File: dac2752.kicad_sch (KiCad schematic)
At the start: 57 parts, among them U61 OPA2388D, U62 OPA2388D, U63 OPA2197xD, U64 OPA2197xD

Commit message: More work in progres
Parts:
- removed C?: 10n, symbol Device:C
- added C?: 100p, symbol Device:C
- C?: value 33n -> 10n
- R? (x2): value 1k -> 3k3
- gave numbers to parts that had none: 15
- renumbered U61 to U32, U63 to U33, U62 to U35, U64 to U36
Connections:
- net -5VS is gone; now on net REFB: U31.35 (REFB)
- net -18V: no longer U301.4 (V-)
- net at R?.1: now also C?.1; no longer C?.2
- net at U31.31 (RINB): now also U34.6 (-)
- net at R?.1, R?.1, U31.32 (RINB): now also U34.7
- net at R?.1, R?.2, U35.1: now also C?.2
- net at R?.1, R?.2, U35.2 (-): now also C?.1
- net Ref5V: now reaches U34.5 (+)
- net Ref5V: now also U34.3 (+)
- net -5VF renamed REFB
- net REFB: now also C?.2; no longer C?.1
- net AGND renamed GND
- net GND: now also U33.3 (+); no longer U36.3 (+)
- net PGND renamed GNDPWR
- net GNDPWR: now also U301.4 (V-), U36.3 (+); no longer U33.3 (+)
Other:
- moved on the sheet: C301, C?, R?, U301C, U32A, U33A, U34B, U35A, U36A

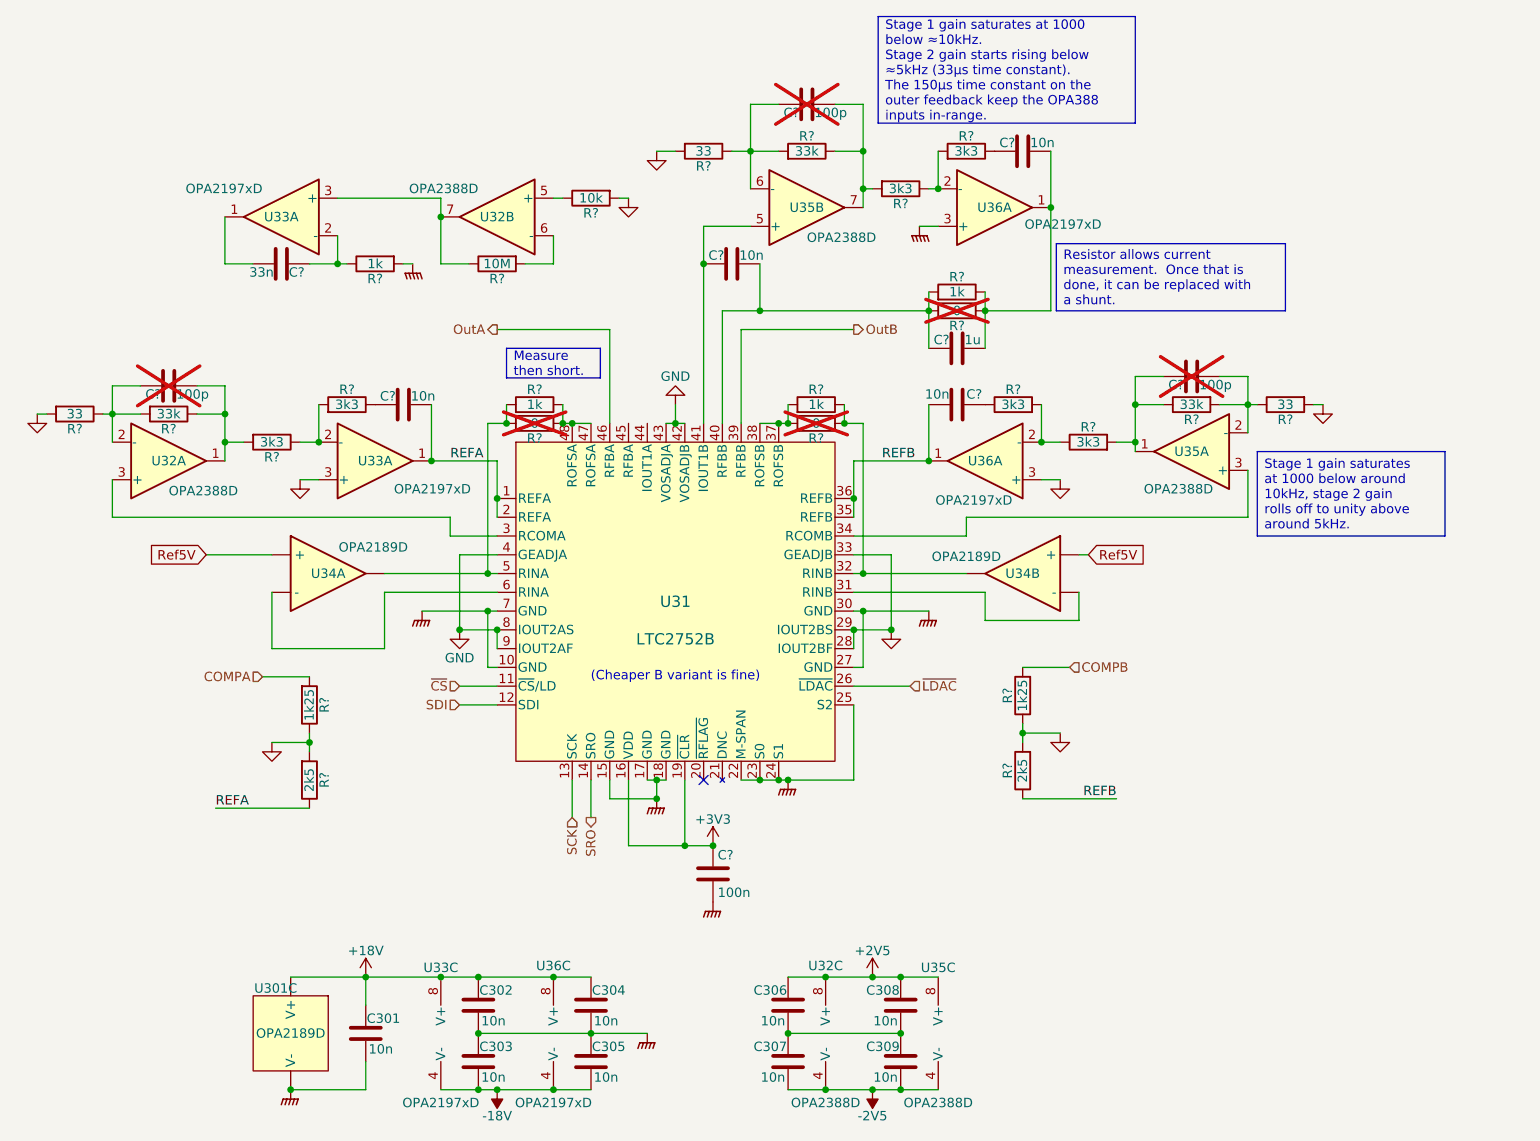
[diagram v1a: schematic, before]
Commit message: Analog side is more or less complete.
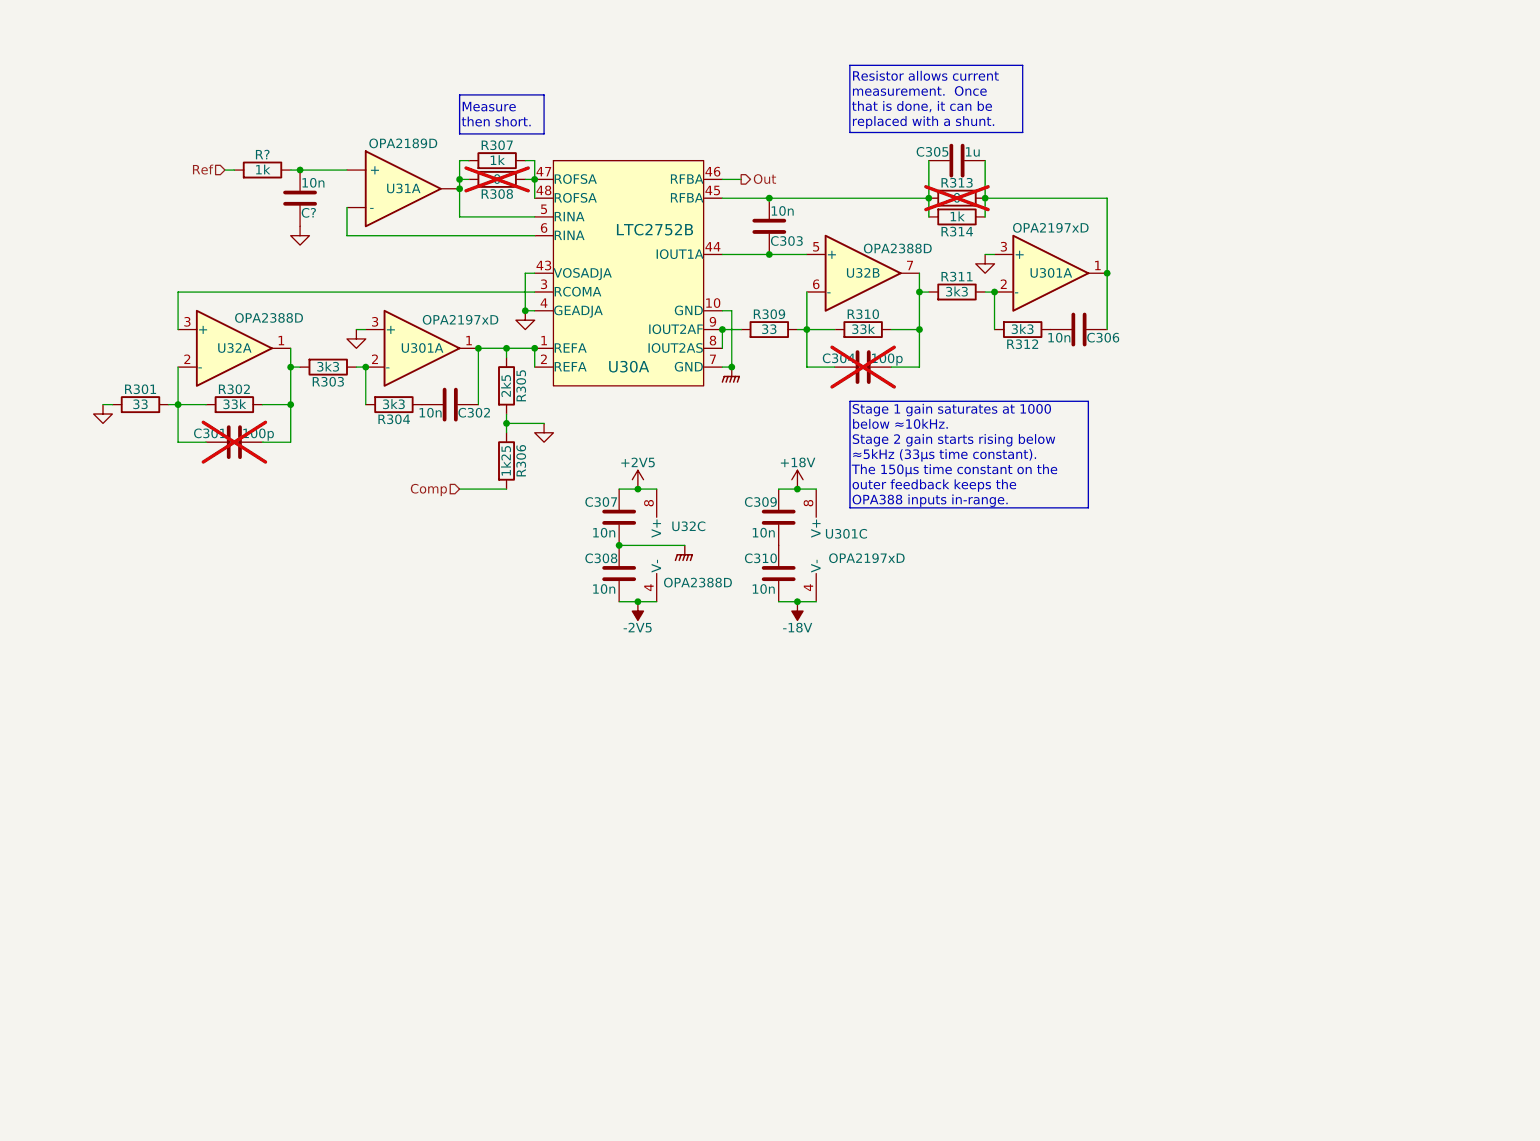
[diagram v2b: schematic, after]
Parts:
- removed C301, C304, C308, C309, C? (x3): 10n, symbol Device:C
- removed C?: 100n, symbol Device:C
- removed C?: 33n, symbol Device:C
- removed C?: 100p, symbol Device:C
- removed C?: 1u, symbol Device:C
- removed R? (x3): 1k, symbol Device:R
- removed R? (x3): 3k3, symbol Device:R
- removed R? (x2): 33k, symbol Device:R
- removed R?: 1k25, symbol Device:R
- removed R?: 10M, symbol Device:R
- removed R?: 33, symbol Device:R
- removed R?: 2k5, symbol Device:R
- removed R?: 10k, symbol Device:R
- removed R? (x2): 0, symbol Device:R
- removed U301: OPA2189D, Package_SO:SOIC-8_3.9x4.9mm_P1.27mm, symbol Parts:OPA2189D
- removed U31: LTC2752B, LQFP-48_LX_LIT, symbol Parts:LTC2752B
- removed unit 2 of U32
- removed unit 1 of U33 (x2)
- removed unit 2 of U34
- removed unit 3 of U35
- removed unit 1 of U35
- removed U36 (x2): OPA2197xD, Package_SO:SOIC-8_3.9x4.9mm_P1.27mm, symbol Amplifier_Operational:OPA2197xD
- added C302, C306, C?: 10n, symbol Device:C
- added R310: 33k, symbol Device:R
- added R312: 3k3, symbol Device:R
- added R313: 0, symbol Device:R
- added R314, R?: 1k, symbol Device:R
- added U30: LTC2752B, Package_QFP:LQFP-48_7x7mm_P0.5mm, symbol Parts:LTC2752B_split
- added unit 1 of U301 (x2)
- C305: value 10n -> 1u
- gave numbers to parts that had none: 13
- renumbered C306 to C307, C307 to C308, C302 to C309, C303 to C310, U33 to U301, U34 to U31, U35 to U32
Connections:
- net -18V: no longer C305.2
- net GND: now also C?.2, U30.4 (GEADJA), U30.43 (VOSADJA), U301.3 (+), U301.3 (+); no longer R309.2
- net GNDPWR: now also C307.2, C308.1, U30.10 (GND), U30.7 (GND); no longer C305.1, C309.2, C310.1
- net at U32.3 (+): now also U30.3 (RCOMA)
- net at R303.1, R304.2: now also U301.2 (-)
- net at C303.1: now also C305.2, R313.2, R314.2, U30.45 (RFBA)
- net at C303.2, U32.5 (+): now also U30.44 (IOUT1A)
- net at C304.2, R309.1, U32.6 (-): now also R310.2
- net at C304.1, R311.2, U32.7: now also R310.1
- net at R307.1, R308.1: now also U30.47 (ROFSA), U30.48 (ROFSA)
- net at R307.2, R308.2, U31.1: now also U30.5 (RINA)
- net at U31.2 (-): now also U30.6 (RINA)
- net at R304.1: now also C302.2
- net at R311.1: now also R312.2, U301.2 (-)
- net COMPA renamed Comp
- net REFA: no longer names the net of R305.1
- net REFA: now also C302.1, U30.1 (REFA), U30.2 (REFA), U301.1
- net Ref5V: no longer names the net of U31.3 (+)
- net Ref5V: now also C?.1, R?.1
- new net: C305.1, C306.1, R313.1, R314.1, U301.1
- new net: R309.2, U30.8 (IOUT2AS), U30.9 (IOUT2AF)
- new net: C309.2, C310.1
- new net: C306.2, R312.1
- new net Out: U30.46 (RFBA)
- new net Ref: R?.2
- no-connect marks 1 -> 0
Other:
- note removed: "(Cheaper B variant is fine)"
- moved on the sheet: C301, C303, C304, C307, C308, C309, C310, R301, R302, R303, R304, R305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

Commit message: Little simplifications etc.
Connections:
- net GND: now also R309.2, U30.8 (IOUT2AS), U30.9 (IOUT2AF)
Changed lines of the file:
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@@
 	(generator_version "9.0")
 	(paper "A4")
+	(text_box "Connect to IOUT2"
+		(exclude_from_sim no)
+		(at 104.9655 81.8459 0)
+		(size 10.6044 4.514)
+		(margins 0.9525 0.9525 0.9525 0.9525)
+		(stroke
+			(width 0)
+			(type default)
+		)
+		(fill
+			(type none)
+		)
+		(effects
+			(font
+				(size 1.27 1.27)
+			)
+			(justify left)
+		)
+	)
 	(text_box "Measure then short."
 		(exclude_from_sim no)
@@
 	)
 	(junction
+		(at 127 73.66)
+		(diameter 0)
+		(color 0 0 0 0)
+	)
+	(junction
 		(at 97.79 83.82)
 		(diameter 0)
@@
 	)
 	(junction
-		(at 128.27 76.2)
-		(diameter 0)
-		(color 0 0 0 0)
-	)
-	(junction
 		(at 163.83 66.04)
 		(diameter 0)
@@
 	(wire
 		(pts
+			(xy 127 73.66) (xy 130.81 73.66)
+		)
+		(stroke
+			(width 0)
+			(type default)
+		)
+	)
+	(wire
+		(pts
 			(xy 149.86 76.2) (xy 153.67 76.2)
 		)
@@
 	(wire
 		(pts
-			(xy 128.27 68.58) (xy 128.27 76.2)
-		)
-		(stroke
-			(width 0)
-			(type default)
-		)
-	)
-	(wire
-		(pts
 			(xy 101.6 68.58) (xy 100.33 68.58)
 		)
@@
 	)
 	(symbol
+		(lib_id "power:GNDPWR")
+		(at 128.27 68.58 0)
+		(unit 1)
+		(exclude_from_sim no)
+		(in_bom yes)
+		(on_board yes)
+		(dnp no)
+		(property "Reference" "#PWR0561"
+			(at 128.27 74.93 0)
+			(effects
+				(font
+					(size 1.27 1.27)
+				)
+				(hide yes)
+			)
+		)
+		(property "Value" "GNDPWR"
+			(at 128.27 71.882 0)
+			(effects
+				(font
+					(size 1.27 1.27)
+				)
+				(hide yes)
+			)
+		)
+		(property "Footprint" ""
+			(at 128.27 69.85 0)
+			(effects
+				(font
+					(size 1.27 1.27)
+				)
+				(hide yes)
+			)
+		)
+		(property "Datasheet" ""
+			(at 128.27 69.85 0)
+			(effects
+				(font
+					(size 1.27 1.27)
+				)
+				(hide yes)
+			)
+		)
+		(property "Description" "Power symbol creates a global label with name \"GNDPWR\" , global ground"
+			(at 128.27 68.58 0)
+			(effects
+				(font
+					(size 1.27 1.27)
+				)
+				(hide yes)
+			)
+		)
+		(pin "1"
+		)
+		(instances
+			(project "lincal"
+				(path "/b054cef4-39e3-49d8-aff0-7ba5a206c187/361a423f-d05f-4f8b-bc28-600b62434109"
+					(reference "#PWR0562")
+					(unit 1)
+				)
+				(path "/b054cef4-39e3-49d8-aff0-7ba5a206c187/460d889b-fb9b-4b3e-8128-6fba79ce7ab4"
+					(reference "#PWR0563")
+					(unit 1)
+				)
+				(path "/b054cef4-39e3-49d8-aff0-7ba5a206c187/aeb3a378-4287-41b1-9e33-8dbd035c4d66"
+					(reference "#PWR0564")
+					(unit 1)
+				)
+				(path "/b054cef4-39e3-49d8-aff0-7ba5a206c187/f2e682f2-52ca-4ed0-8a7d-aeb09fbc9914"
+					(reference "#PWR0561")
+					(unit 1)
+				)
+			)
+		)
+	)
+	(symbol
 		(lib_id "Device:R")
 		(at 97.79 78.74 0)
@@
 					(unit 1)
 				)
+			)
+		)
+	)
+	(symbol
+		(lib_id "power:GND")
+		(at 130.81 73.66 0)
+		(mirror y)
+		(unit 1)
+		(exclude_from_sim no)
+		(in_bom yes)
+		(on_board yes)
+		(dnp no)
+		(property "Reference" "#PWR0565"
+			(at 130.81 80.01 0)
+			(effects
+				(font
+					(size 1.27 1.27)
+				)
+				(hide yes)
+			)
+		)
+		(property "Value" "GND"
+			(at 130.81 77.47 0)
+			(effects
+				(font
+					(size 1.27 1.27)
+				)
+				(hide yes)
+			)
+		)
+		(property "Footprint" ""
+			(at 130.81 73.66 0)
+			(effects
+				(font
+					(size 1.27 1.27)
+				)
+				(hide yes)
+			)
+		)
+		(property "Datasheet" ""
+			(at 130.81 73.66 0)
+			(effects
+				(font
+					(size 1.27 1.27)
+				)
+				(hide yes)
+			)
+		)
+		(property "Description" "Power symbol creates a global label with name \"GND\" , ground"
+			(at 130.81 73.66 0)
+			(effects
+				(font
+					(size 1.27 1.27)
+				)
+				(hide yes)
+			)
+		)
+		(pin "1"
+		)
+		(instances
+			(project "lincal"
+				(path "/b054cef4-39e3-49d8-aff0-7ba5a206c187/361a423f-d05f-4f8b-bc28-600b62434109"
+					(reference "#PWR0566")
+					(unit 1)
+				)
+				(path "/b054cef4-39e3-49d8-aff0-7ba5a206c187/460d889b-fb9b-4b3e-8128-6fba79ce7ab4"
+					(reference "#PWR0567")
+					(unit 1)
+				)
+				(path "/b054cef4-39e3-49d8-aff0-7ba5a206c187/aeb3a378-4287-41b1-9e33-8dbd035c4d66"
+					(reference "#PWR0568")
+					(unit 1)
+				)
+				(path "/b054cef4-39e3-49d8-aff0-7ba5a206c187/f2e682f2-52ca-4ed0-8a7d-aeb09fbc9914"
+					(reference "#PWR0565")
+					(unit 1)
+				)

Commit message: Schematic complete, maybe
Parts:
- removed C305: 1u, symbol Device:C
- added C313: 10n, Capacitor_SMD:C_0603_1608Metric, symbol Device:C
- C301, C304: footprint (none) -> Capacitor_SMD:C_0603_1608Metric; now left out of the parts list
- C302, C303, C306: footprint (none) -> Capacitor_SMD:C_0603_1608Metric; LCSC (none) -> C307500
- C307, C308, C309, C310: value 10n -> 0u1; footprint (none) -> Capacitor_SMD:C_0402_1005Metric; LCSC (none) -> C307331
- C311: renamed from C?; footprint (none) -> Capacitor_SMD:C_0603_1608Metric; LCSC (none) -> C307500
- R307, R308, R313, R314: footprint (none) -> Resistor_SMD:R_0603_1608Metric
- U301: LCSC (none) -> C139363; now left out of the parts list
- U31: LCSC (none) -> C881489; now left out of the parts list
- U32: LCSC (none) -> C1517414
- gave numbers to parts that had none: 1
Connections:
- net GND: now also U301.5 (+); no longer U301.3 (+)
- net at C306.1, R313.1, R314.1: now also U301.7; no longer U301.1
- net at R311.1, R312.2: now also U301.6 (-); no longer U301.2 (-)
- net at R307.2, R308.2, U30.5 (RINA)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: now also C313.1
- net at U30.6 (RINA), U31.2 (-): now also C313.2
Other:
- moved on the sheet: C311, R314, R315, U31A

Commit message: Part selection
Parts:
- R301, R309: footprint (none) -> Resistor_SMD:R_0603_1608Metric; LCSC (none) -> C23140
- R302, R310: footprint (none) -> Resistor_SMD:R_0603_1608Metric; LCSC (none) -> C4216
- R303, R304, R311, R312: footprint (none) -> Resistor_SMD:R_0603_1608Metric; LCSC (none) -> C22978
- R305: value 2k5 -> 2k4; footprint (none) -> Resistor_SMD:R_0402_1005Metric; LCSC (none) -> C25882
- R306: value 1k25 -> 1k2; footprint (none) -> Resistor_SMD:R_0402_1005Metric; LCSC (none) -> C25862
- R307, R314: footprint Resistor_SMD:R_0603_1608Metric -> Resistor_SMD:R_0402_1005Metric; LCSC (none) -> C11702
- R308, R313: now left out of the parts list
- R315: footprint (none) -> Resistor_SMD:R_0402_1005Metric; LCSC (none) -> C11702
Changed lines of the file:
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@@
 			)
 		)
-		(property "Footprint" ""
+		(property "Footprint" "Resistor_SMD:R_0603_1608Metric"
 			(at 73.66 74.422 90)
 			(effects
@@
 			)
 		)
+		(property "LCSC" "C22978"
+			(at 73.66 76.2 90)
+			(effects
+				(font
+					(size 1.27 1.27)
+				)
+				(hide yes)
+			)
+		)
 		(pin "2"
 		)
@@
 		(unit 1)
 		(exclude_from_sim no)
-		(in_bom yes)
+		(in_bom no)
 		(on_board yes)
 		(dnp yes)
@@
 			)
 		)
-		(property "Footprint" "Resistor_SMD:R_0603_1608Metric"
+		(property "Footprint" "Resistor_SMD:R_0402_1005Metric"
 			(at 96.52 50.038 90)
 			(effects
@@
 			)
 		)
-		(property "Datasheet" "shunt"
+		(property "Datasheet" "~"
 			(at 96.52 48.26 0)
 			(effects
@@
 			)
 		)
+		(property "LCSC" "C11702"
+			(at 96.52 48.26 90)
+			(effects
+				(font
+					(size 1.27 1.27)
+				)
+				(hide yes)
+			)
+		)
 		(pin "2"
 		)
@@
 			)
 		)
-		(property "Footprint" ""
+		(property "Footprint" "Resistor_SMD:R_0603_1608Metric"
 			(at 82.55 79.502 90)
 			(effects
@@
 			)
 		)
+		(property "LCSC" "C22978"
+			(at 82.55 81.28 90)
+			(effects
+				(font
+					(size 1.27 1.27)
+				)
+				(hide yes)
+			)
+		)
 		(pin "2"
 		)
@@
 			)
 		)
-		(property "Footprint" ""
+		(property "Footprint" "Resistor_SMD:R_0603_1608Metric"
 			(at 48.26 83.058 90)
 			(effects
@@
 			)
 		)
+		(property "LCSC" "C23140"
+			(at 48.26 81.28 90)
+			(effects
+				(font
+					(size 1.27 1.27)
+				)
+				(hide yes)
+			)
+		)
 		(pin "2"
 		)
@@
 			)
 		)
-		(property "Footprint" ""
+		(property "Footprint" "Resistor_SMD:R_0603_1608Metric"
 			(at 60.96 83.058 90)
 			(effects
@@
 			)
 		)
+		(property "LCSC" "C4216"
+			(at 60.96 81.28 90)
+			(effects
+				(font
+					(size 1.27 1.27)
+				)
+				(hide yes)
+			)
+		)
 		(pin "2"
 		)
@@
 			)
 		)
-		(property "Footprint" "Resistor_SMD:R_0603_1608Metric"
+		(property "Footprint" "Resistor_SMD:R_0402_1005Metric"
 			(at 158.75 52.578 90)
 			(effects
@@
 			)
 		)
-		(property "Datasheet" "shunt"
+		(property "Datasheet" "~"
 			(at 158.75 50.8 0)
 			(effects
@@
 			)
 		)
+		(property "LCSC" "C11702"
+			(at 158.75 50.8 90)
+			(effects
+				(font
+					(size 1.27 1.27)
+				)
+				(hide yes)
+			)
+		)
 		(pin "2"
 		)
@@
 			)
 		)
-		(property "Footprint" ""
+		(property "Footprint" "Resistor_SMD:R_0603_1608Metric"
 			(at 167.64 69.342 90)
 			(effects
@@
 			)
 		)
+		(property "LCSC" "C22978"
+			(at 167.64 71.12 90)
+			(effects
+				(font
+					(size 1.27 1.27)
+				)
+				(hide yes)
+			)
+		)
 		(pin "2"
 		)
@@
 		(unit 1)
 		(exclude_from_sim no)
-		(in_bom yes)
+		(in_bom no)
 		(on_board yes)
 		(dnp yes)
@@
 			)
 		)
-		(property "Footprint" ""
+		(property "Footprint" "Resistor_SMD:R_0603_1608Metric"
 			(at 133.35 72.898 90)
 			(effects
@@
 			)
 		)
-		(property "Datasheet" "Thin film or foil?"
+		(property "Datasheet" "Easy swap"
 			(at 133.35 71.12 0)
 			(effects
@@
 			)
 		)
+		(property "LCSC" "C23140"
+			(at 133.35 71.12 90)
+			(effects
+				(font
+					(size 1.27 1.27)
+				)
+				(hide yes)
+			)
+		)
 		(pin "2"
 		)
@@
 			)
 		)
-		(property "Footprint" ""
+		(property "Footprint" "Resistor_SMD:R_0603_1608Metric"
 			(at 158.75 67.818 90)
 			(effects
@@
 			)
 		)
+		(property "LCSC" "C22978"
+			(at 158.75 66.04 90)
+			(effects
+				(font
+					(size 1.27 1.27)
+				)
+				(hide yes)
+			)
+		)
 		(pin "2"
 		)
@@
 			)
 		)
-		(property "Footprint" ""
+		(property "Footprint" "Resistor_SMD:R_0402_1005Metric"
 			(at 59.69 50.038 90)
 			(effects
@@
 			)
 		)
+		(property "LCSC" "C11702"
+			(at 59.69 48.26 90)
+			(effects
+				(font
+					(size 1.27 1.27)
+				)
+				(hide yes)
+			)
+		)
 		(pin "2"
 		)
@@
 			)
 		)
-		(property "Value" "2k5"
+		(property "Value" "2k4"
 			(at 97.79 78.74 90)
 			(effects
@@
 			)
 		)
-		(property "Footprint" ""
+		(property "Footprint" "Resistor_SMD:R_0402_1005Metric"
 			(at 96.012 78.74 90)
 			(effects
@@
 			)
 		)
-		(property "Datasheet" "Thin film or foil?"
+		(property "Datasheet" "~"
 			(at 97.79 78.74 0)
 			(effects
@@
 			)
 		)
+		(property "LCSC" "C25882"
+			(at 97.79 78.74 90)
+			(effects
+				(font
+					(size 1.27 1.27)
+				)
+				(hide yes)
+			)
+		)
 		(pin "2"
 		)
@@
 			)
 		)
-		(property "Footprint" ""
+		(property "Footprint" "Resistor_SMD:R_0603_1608Metric"
 			(at 146.05 72.898 90)
 			(effects
@@
 			)
 		)
-		(property "Datasheet" "Thin film or foil?"
+		(property "Datasheet" "Easy swap"
 			(at 146.05 71.12 0)
 			(effects
@@
 			)
 		)
+		(property "LCSC" "C4216"
+			(at 146.05 71.12 90)
+			(effects
+				(font
+					(size 1.27 1.27)
+				)
+				(hide yes)
+			)
+		)
 		(pin "2"
 		)
@@
 			)
 		)
-		(property "Value" "1k25"
+		(property "Value" "1k2"
 			(at 97.79 88.9 90)
 			(effects
@@
 			)
 		)
-		(property "Footprint" ""
+		(property "Footprint" "Resistor_SMD:R_0402_1005Metric"
 			(at 96.012 88.9 90)
 			(effects
@@
 			)
 		)
-		(property "Datasheet" "Thin film or foil?"
+		(property "Datasheet" "~"
 			(at 97.79 88.9 0)
 			(effects
@@
 			(effects
 				(font
+					(size 1.27 1.27)
+				)
+				(hide yes)
+			)
+		)
+		(property "LCSC" "C25862"
+			(at 97.79 88.9 90)
+			(effects
+				(font

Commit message: ERC passes.
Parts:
- C301, C304: value 100p -> 0n1
- R315: value 1k -> 100; LCSC C11702 -> (none)
- U301: value OPA2197xD -> OPA2197D
- U31: value OPA2189D -> OPA2189DGK; footprint Package_SO:SOIC-8_3.9x4.9mm_P1.27mm -> Package_SO:MSOP-8_3x3mm_P0.65mm; symbol Parts:OPA2189D -> Parts:OPA2189DGK
- U32: value OPA2388D -> OPA2388DGK; footprint Package_SO:SOIC-8_3.9x4.9mm_P1.27mm -> Package_SO:MSOP-8_3x3mm_P0.65mm; symbol Parts:OPA2388D -> Parts:OPA2388DGK; now left out of the parts list
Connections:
- net GNDPWR: now also C309.2, C310.1; no longer U30.10 (GND), U30.7 (GND)
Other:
- moved on the sheet: C303, C304, C306, R309, R310, R311, R312, R313, R314
